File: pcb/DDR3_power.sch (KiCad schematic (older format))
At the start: 14 parts

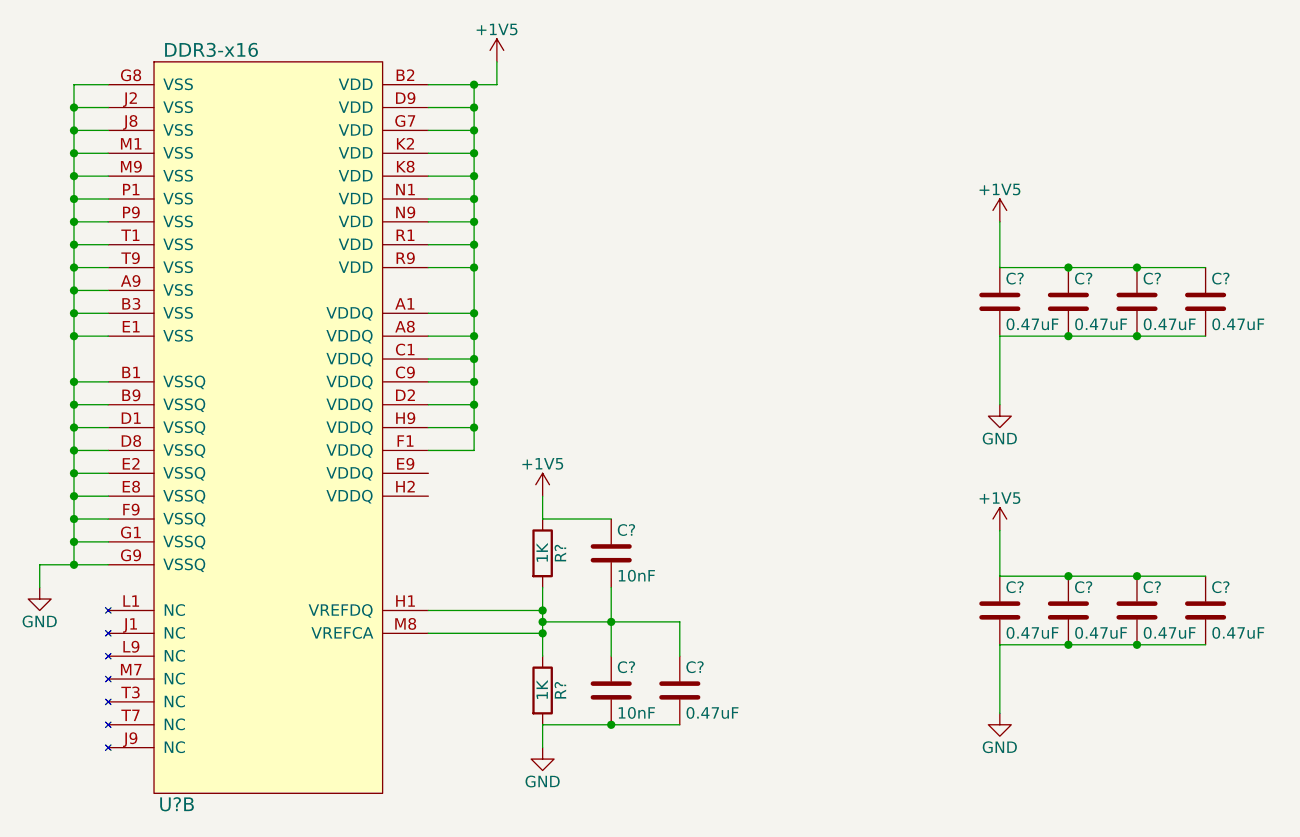
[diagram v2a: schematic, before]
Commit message: Added part numbers and updated schematic
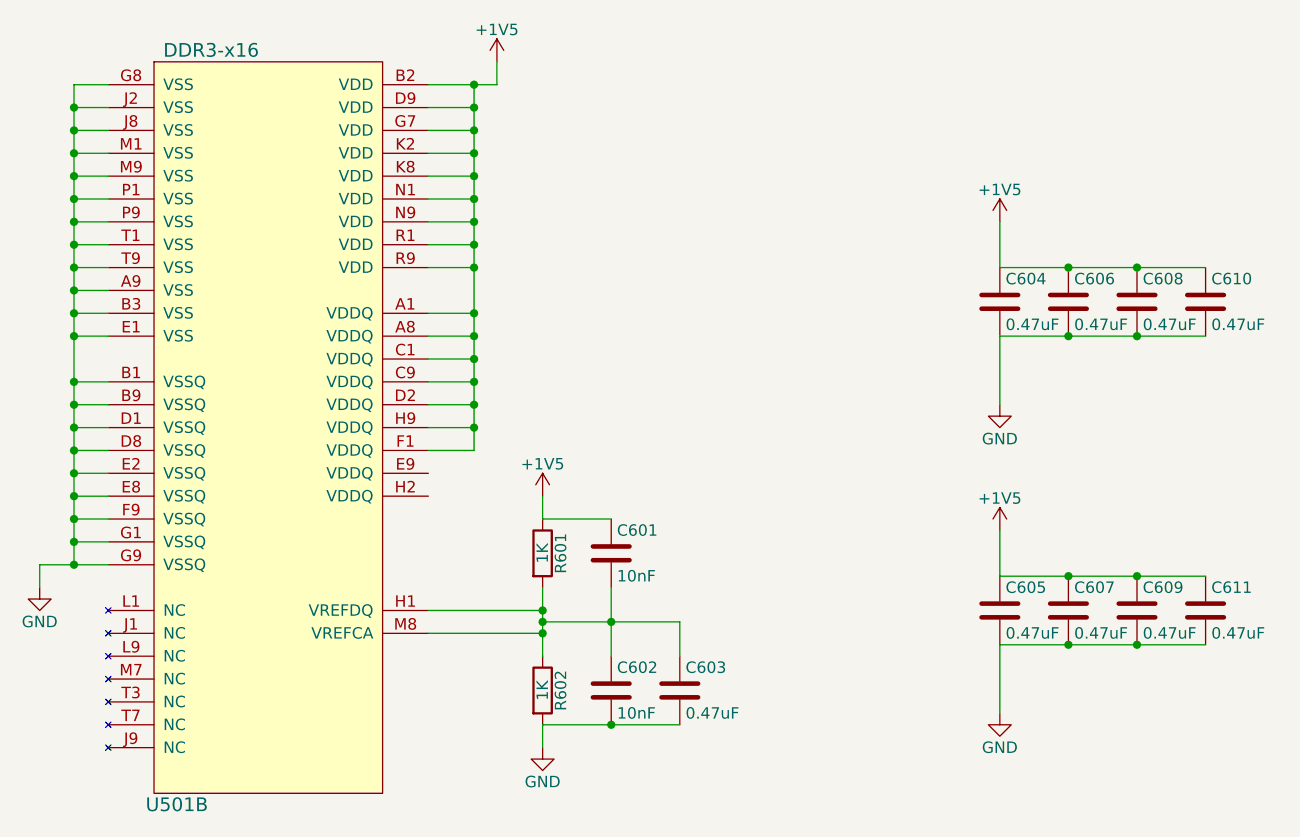
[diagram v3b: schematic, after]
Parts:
- gave numbers to parts that had none: 14
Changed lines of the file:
@@
 $EndDescr
 $Comp
-L DDR3-x16 U?
+L DDR3-x16 U501
 U 2 1 561B3BA2
 P 4900 3500
-F 0 "U?" H 4500 1850 60  0000 C CNN
+F 0 "U501" H 4500 1850 60  0000 C CNN
 F 1 "DDR3-x16" H 4650 5150 60  0000 C CNN
 F 2 "" H 4900 3100 60  0000 C CNN
@@
 Connection ~ 5800 2100
 $Comp
-L R R?
+L R R601
 U 1 1 561BF16C
 P 6100 4050
-F 0 "R?" V 6180 4050 50  0000 C CNN
+F 0 "R601" V 6180 4050 50  0000 C CNN
 F 1 "1K" V 6100 4050 50  0000 C CNN
 F 2 "" V 6030 4050 30  0000 C CNN
@@
 $EndComp
 $Comp
-L R R?
+L R R602
 U 1 1 561BF1C9
 P 6100 4650
-F 0 "R?" V 6180 4650 50  0000 C CNN
+F 0 "R602" V 6180 4650 50  0000 C CNN
 F 1 "1K" V 6100 4650 50  0000 C CNN
 F 2 "" V 6030 4650 30  0000 C CNN
@@
 $EndComp
 $Comp
-L C C?
+L C C601
 U 1 1 561BF214
 P 6400 4050
-F 0 "C?" H 6425 4150 50  0000 L CNN
+F 0 "C601" H 6425 4150 50  0000 L CNN
 F 1 "10nF" H 6425 3950 50  0000 L CNN
 F 2 "" H 6438 3900 30  0000 C CNN
@@
 $EndComp
 $Comp
-L C C?
+L C C602
 U 1 1 561BF25B
 P 6400 4650
-F 0 "C?" H 6425 4750 50  0000 L CNN
+F 0 "C602" H 6425 4750 50  0000 L CNN
 F 1 "10nF" H 6425 4550 50  0000 L CNN
 F 2 "" H 6438 4500 30  0000 C CNN
@@
 $EndComp
 $Comp
-L C C?
+L C C603
 U 1 1 561BF2A8
 P 6700 4650
-F 0 "C?" H 6725 4750 50  0000 L CNN
+F 0 "C603" H 6725 4750 50  0000 L CNN
 F 1 "0.47uF" H 6725 4550 50  0000 L CNN
 F 2 "" H 6738 4500 30  0000 C CNN
@@
 $EndComp
 $Comp
-L GND #PWR?
+L GND #PWR601
 U 1 1 561BF2F5
 P 3900 4200
-F 0 "#PWR?" H 3900 3950 50  0001 C CNN
+F 0 "#PWR601" H 3900 3950 50  0001 C CNN
 F 1 "GND" H 3900 4050 50  0000 C CNN
 F 2 "" H 3900 4200 60  0000 C CNN
@@
 $EndComp
 $Comp
-L GND #PWR?
+L GND #PWR604
 U 1 1 561BF315
 P 6100 4900
-F 0 "#PWR?" H 6100 4650 50  0001 C CNN
+F 0 "#PWR604" H 6100 4650 50  0001 C CNN
 F 1 "GND" H 6100 4750 50  0000 C CNN
 F 2 "" H 6100 4900 60  0000 C CNN
@@
 $EndComp
 $Comp
-L +1V5 #PWR?
+L +1V5 #PWR602
 U 1 1 561BF335
 P 5900 1900
-F 0 "#PWR?" H 5900 1750 50  0001 C CNN
+F 0 "#PWR602" H 5900 1750 50  0001 C CNN
 F 1 "+1V5" H 5900 2040 50  0000 C CNN
 F 2 "" H 5900 1900 60  0000 C CNN
@@
 $EndComp
 $Comp
-L +1V5 #PWR?
+L +1V5 #PWR603
 U 1 1 561BF355
 P 6100 3800
-F 0 "#PWR?" H 6100 3650 50  0001 C CNN
+F 0 "#PWR603" H 6100 3650 50  0001 C CNN
 F 1 "+1V5" H 6100 3940 50  0000 C CNN
 F 2 "" H 6100 3800 60  0000 C CNN
@@
 $EndComp
 $Comp
-L +1V5 #PWR?
+L +1V5 #PWR605
 U 1 1 561BF375
 P 8100 2600
-F 0 "#PWR?" H 8100 2450 50  0001 C CNN
+F 0 "#PWR605" H 8100 2450 50  0001 C CNN
 F 1 "+1V5" H 8100 2740 50  0000 C CNN
 F 2 "" H 8100 2600 60  0000 C CNN
@@
 $EndComp
 $Comp
-L GND #PWR?
+L GND #PWR606
 U 1 1 561BF395
 P 8100 3400
-F 0 "#PWR?" H 8100 3150 50  0001 C CNN
+F 0 "#PWR606" H 8100 3150 50  0001 C CNN
 F 1 "GND" H 8100 3250 50  0000 C CNN
 F 2 "" H 8100 3400 60  0000 C CNN
@@
 $EndComp
 $Comp
-L C C?
+L C C604
 U 1 1 561BF3B5
 P 8100 2950
-F 0 "C?" H 8125 3050 50  0000 L CNN
+F 0 "C604" H 8125 3050 50  0000 L CNN
 F 1 "0.47uF" H 8125 2850 50  0000 L CNN
 F 2 "" H 8138 2800 30  0000 C CNN
@@
 $EndComp
 $Comp
-L C C?
+L C C606
 U 1 1 561BF426
 P 8400 2950
-F 0 "C?" H 8425 3050 50  0000 L CNN
+F 0 "C606" H 8425 3050 50  0000 L CNN
 F 1 "0.47uF" H 8425 2850 50  0000 L CNN
 F 2 "" H 8438 2800 30  0000 C CNN
@@
 $EndComp
 $Comp
-L C C?
+L C C608
 U 1 1 561BF471
 P 8700 2950
-F 0 "C?" H 8725 3050 50  0000 L CNN
+F 0 "C608" H 8725 3050 50  0000 L CNN
 F 1 "0.47uF" H 8725 2850 50  0000 L CNN
 F 2 "" H 8738 2800 30  0000 C CNN
@@
 $EndComp
 $Comp
-L C C?
+L C C610
 U 1 1 561BF4DA
 P 9000 2950
-F 0 "C?" H 9025 3050 50  0000 L CNN
+F 0 "C610" H 9025 3050 50  0000 L CNN
 F 1 "0.47uF" H 9025 2850 50  0000 L CNN
 F 2 "" H 9038 2800 30  0000 C CNN
@@
 Connection ~ 4050 4100
 $Comp
-L +1V5 #PWR?
+L +1V5 #PWR607
 U 1 1 561C70D7
 P 8100 3950
-F 0 "#PWR?" H 8100 3800 50  0001 C CNN
+F 0 "#PWR607" H 8100 3800 50  0001 C CNN
 F 1 "+1V5" H 8100 4090 50  0000 C CNN
 F 2 "" H 8100 3950 60  0000 C CNN
@@
 $EndComp
 $Comp
-L GND #PWR?
+L GND #PWR608
 U 1 1 561C70DD
 P 8100 4750
-F 0 "#PWR?" H 8100 4500 50  0001 C CNN
+F 0 "#PWR608" H 8100 4500 50  0001 C CNN
 F 1 "GND" H 8100 4600 50  0000 C CNN
 F 2 "" H 8100 4750 60  0000 C CNN
@@
 $EndComp
 $Comp
-L C C?
+L C C605
 U 1 1 561C70E3
 P 8100 4300
-F 0 "C?" H 8125 4400 50  0000 L CNN
+F 0 "C605" H 8125 4400 50  0000 L CNN
 F 1 "0.47uF" H 8125 4200 50  0000 L CNN
 F 2 "" H 8138 4150 30  0000 C CNN
@@
 $EndComp
 $Comp
-L C C?
+L C C607
 U 1 1 561C70E9
 P 8400 4300
-F 0 "C?" H 8425 4400 50  0000 L CNN
+F 0 "C607" H 8425 4400 50  0000 L CNN
 F 1 "0.47uF" H 8425 4200 50  0000 L CNN
 F 2 "" H 8438 4150 30  0000 C CNN
@@
 $EndComp
 $Comp
-L C C?
+L C C609
 U 1 1 561C70EF
 P 8700 4300
-F 0 "C?" H 8725 4400 50  0000 L CNN
+F 0 "C609" H 8725 4400 50  0000 L CNN
 F 1 "0.47uF" H 8725 4200 50  0000 L CNN
 F 2 "" H 8738 4150 30  0000 C CNN
@@
 $EndComp
 $Comp
-L C C?
+L C C611
 U 1 1 561C70F5
 P 9000 4300
-F 0 "C?" H 9025 4400 50  0000 L CNN
+F 0 "C611" H 9025 4400 50  0000 L CNN
 F 1 "0.47uF" H 9025 4200 50  0000 L CNN
 F 2 "" H 9038 4150 30  0000 C CNN

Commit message: mostly done with component placement
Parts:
- C601, C602, C603, C604, C605, C606, C607, C608, C609, C610, C611: footprint (none) -> wbraun_smd:C_0402
- R601, R602: footprint (none) -> wbraun_smd:R_0402
- U501: footprint (none) -> wbraun_smd:FBGA-96-DDR3-SDRAM
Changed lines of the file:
@@
 F 0 "U501" H 4500 1850 60  0000 C CNN
 F 1 "DDR3-x16" H 4650 5150 60  0000 C CNN
-F 2 "" H 4900 3100 60  0000 C CNN
+F 2 "wbraun_smd:FBGA-96-DDR3-SDRAM" H 4900 3100 60  0001 C CNN
 F 3 "" H 4900 3100 60  0000 C CNN
 	2    4900 3500
@@
 F 0 "R601" V 6180 4050 50  0000 C CNN
 F 1 "1K" V 6100 4050 50  0000 C CNN
-F 2 "" V 6030 4050 30  0000 C CNN
+F 2 "wbraun_smd:R_0402" V 6030 4050 30  0001 C CNN
 F 3 "" H 6100 4050 30  0000 C CNN
 	1    6100 4050
@@
 F 0 "R602" V 6180 4650 50  0000 C CNN
 F 1 "1K" V 6100 4650 50  0000 C CNN
-F 2 "" V 6030 4650 30  0000 C CNN
+F 2 "wbraun_smd:R_0402" V 6030 4650 30  0001 C CNN
 F 3 "" H 6100 4650 30  0000 C CNN
 	1    6100 4650
@@
 F 0 "C601" H 6425 4150 50  0000 L CNN
 F 1 "10nF" H 6425 3950 50  0000 L CNN
-F 2 "" H 6438 3900 30  0000 C CNN
+F 2 "wbraun_smd:C_0402" H 6438 3900 30  0001 C CNN
 F 3 "" H 6400 4050 60  0000 C CNN
 	1    6400 4050
@@
 F 0 "C602" H 6425 4750 50  0000 L CNN
 F 1 "10nF" H 6425 4550 50  0000 L CNN
-F 2 "" H 6438 4500 30  0000 C CNN
+F 2 "wbraun_smd:C_0402" H 6438 4500 30  0001 C CNN
 F 3 "" H 6400 4650 60  0000 C CNN
 	1    6400 4650
@@
 F 0 "C603" H 6725 4750 50  0000 L CNN
 F 1 "0.47uF" H 6725 4550 50  0000 L CNN
-F 2 "" H 6738 4500 30  0000 C CNN
+F 2 "wbraun_smd:C_0402" H 6738 4500 30  0001 C CNN
 F 3 "" H 6700 4650 60  0000 C CNN
 	1    6700 4650
@@
 $EndComp
 $Comp
-L GND #PWR601
+L GND #PWR081
 U 1 1 561BF2F5
 P 3900 4200
-F 0 "#PWR601" H 3900 3950 50  0001 C CNN
+F 0 "#PWR081" H 3900 3950 50  0001 C CNN
 F 1 "GND" H 3900 4050 50  0000 C CNN
 F 2 "" H 3900 4200 60  0000 C CNN
@@
 $EndComp
 $Comp
-L GND #PWR604
+L GND #PWR082
 U 1 1 561BF315
 P 6100 4900
-F 0 "#PWR604" H 6100 4650 50  0001 C CNN
+F 0 "#PWR082" H 6100 4650 50  0001 C CNN
 F 1 "GND" H 6100 4750 50  0000 C CNN
 F 2 "" H 6100 4900 60  0000 C CNN
@@
 $EndComp
 $Comp
-L +1V5 #PWR602
+L +1V5 #PWR083
 U 1 1 561BF335
 P 5900 1900
-F 0 "#PWR602" H 5900 1750 50  0001 C CNN
+F 0 "#PWR083" H 5900 1750 50  0001 C CNN
 F 1 "+1V5" H 5900 2040 50  0000 C CNN
 F 2 "" H 5900 1900 60  0000 C CNN
@@
 $EndComp
 $Comp
-L +1V5 #PWR603
+L +1V5 #PWR084
 U 1 1 561BF355
 P 6100 3800
-F 0 "#PWR603" H 6100 3650 50  0001 C CNN
+F 0 "#PWR084" H 6100 3650 50  0001 C CNN
 F 1 "+1V5" H 6100 3940 50  0000 C CNN
 F 2 "" H 6100 3800 60  0000 C CNN
@@
 $EndComp
 $Comp
-L +1V5 #PWR605
+L +1V5 #PWR085
 U 1 1 561BF375
 P 8100 2600
-F 0 "#PWR605" H 8100 2450 50  0001 C CNN
+F 0 "#PWR085" H 8100 2450 50  0001 C CNN
 F 1 "+1V5" H 8100 2740 50  0000 C CNN
 F 2 "" H 8100 2600 60  0000 C CNN
@@
 $EndComp
 $Comp
-L GND #PWR606
+L GND #PWR086
 U 1 1 561BF395
 P 8100 3400
-F 0 "#PWR606" H 8100 3150 50  0001 C CNN
+F 0 "#PWR086" H 8100 3150 50  0001 C CNN
 F 1 "GND" H 8100 3250 50  0000 C CNN
 F 2 "" H 8100 3400 60  0000 C CNN
@@
 F 0 "C604" H 8125 3050 50  0000 L CNN
 F 1 "0.47uF" H 8125 2850 50  0000 L CNN
-F 2 "" H 8138 2800 30  0000 C CNN
+F 2 "wbraun_smd:C_0402" H 8138 2800 30  0001 C CNN
 F 3 "" H 8100 2950 60  0000 C CNN
 	1    8100 2950
@@
 F 0 "C606" H 8425 3050 50  0000 L CNN
 F 1 "0.47uF" H 8425 2850 50  0000 L CNN
-F 2 "" H 8438 2800 30  0000 C CNN
+F 2 "wbraun_smd:C_0402" H 8438 2800 30  0001 C CNN
 F 3 "" H 8400 2950 60  0000 C CNN
 	1    8400 2950
@@
 F 0 "C608" H 8725 3050 50  0000 L CNN
 F 1 "0.47uF" H 8725 2850 50  0000 L CNN
-F 2 "" H 8738 2800 30  0000 C CNN
+F 2 "wbraun_smd:C_0402" H 8738 2800 30  0001 C CNN
 F 3 "" H 8700 2950 60  0000 C CNN
 	1    8700 2950
@@
 F 0 "C610" H 9025 3050 50  0000 L CNN
 F 1 "0.47uF" H 9025 2850 50  0000 L CNN
-F 2 "" H 9038 2800 30  0000 C CNN
+F 2 "wbraun_smd:C_0402" H 9038 2800 30  0001 C CNN
 F 3 "" H 9000 2950 60  0000 C CNN
 	1    9000 2950
@@
 Connection ~ 4050 4100
 $Comp
-L +1V5 #PWR607
+L +1V5 #PWR087
 U 1 1 561C70D7
 P 8100 3950
-F 0 "#PWR607" H 8100 3800 50  0001 C CNN
+F 0 "#PWR087" H 8100 3800 50  0001 C CNN
 F 1 "+1V5" H 8100 4090 50  0000 C CNN
 F 2 "" H 8100 3950 60  0000 C CNN
@@
 $EndComp
 $Comp
-L GND #PWR608
+L GND #PWR088
 U 1 1 561C70DD
 P 8100 4750
-F 0 "#PWR608" H 8100 4500 50  0001 C CNN
+F 0 "#PWR088" H 8100 4500 50  0001 C CNN
 F 1 "GND" H 8100 4600 50  0000 C CNN
 F 2 "" H 8100 4750 60  0000 C CNN
@@
 F 0 "C605" H 8125 4400 50  0000 L CNN
 F 1 "0.47uF" H 8125 4200 50  0000 L CNN
-F 2 "" H 8138 4150 30  0000 C CNN
+F 2 "wbraun_smd:C_0402" H 8138 4150 30  0001 C CNN
 F 3 "" H 8100 4300 60  0000 C CNN
 	1    8100 4300
@@
 F 0 "C607" H 8425 4400 50  0000 L CNN
 F 1 "0.47uF" H 8425 4200 50  0000 L CNN
-F 2 "" H 8438 4150 30  0000 C CNN
+F 2 "wbraun_smd:C_0402" H 8438 4150 30  0001 C CNN
 F 3 "" H 8400 4300 60  0000 C CNN
 	1    8400 4300
@@
 F 0 "C609" H 8725 4400 50  0000 L CNN
 F 1 "0.47uF" H 8725 4200 50  0000 L CNN
-F 2 "" H 8738 4150 30  0000 C CNN
+F 2 "wbraun_smd:C_0402" H 8738 4150 30  0001 C CNN
 F 3 "" H 8700 4300 60  0000 C CNN
 	1    8700 4300
@@
 F 0 "C611" H 9025 4400 50  0000 L CNN
 F 1 "0.47uF" H 9025 4200 50  0000 L CNN
-F 2 "" H 9038 4150 30  0000 C CNN
+F 2 "wbraun_smd:C_0402" H 9038 4150 30  0001 C CNN
 F 3 "" H 9000 4300 60  0000 C CNN
 	1    9000 4300

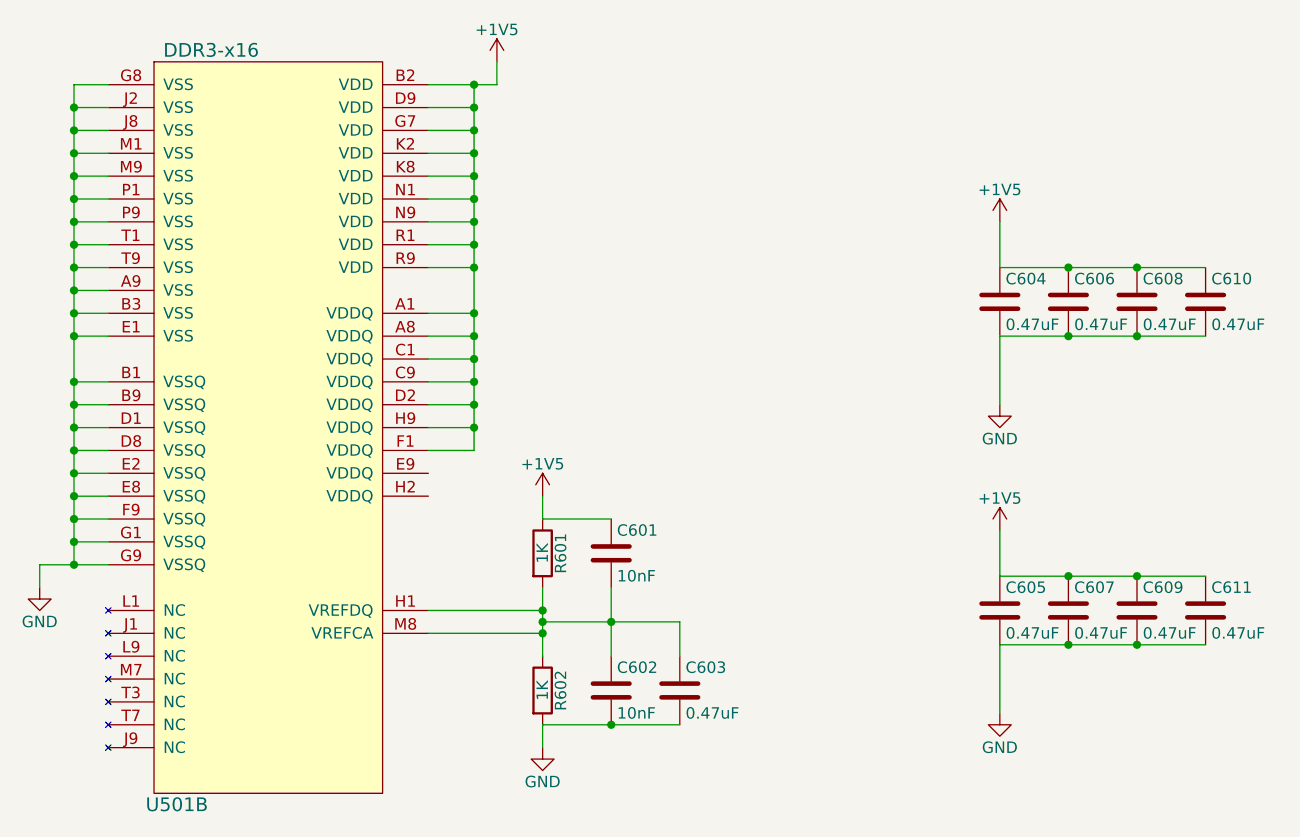
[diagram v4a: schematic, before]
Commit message: DDR routing test 1
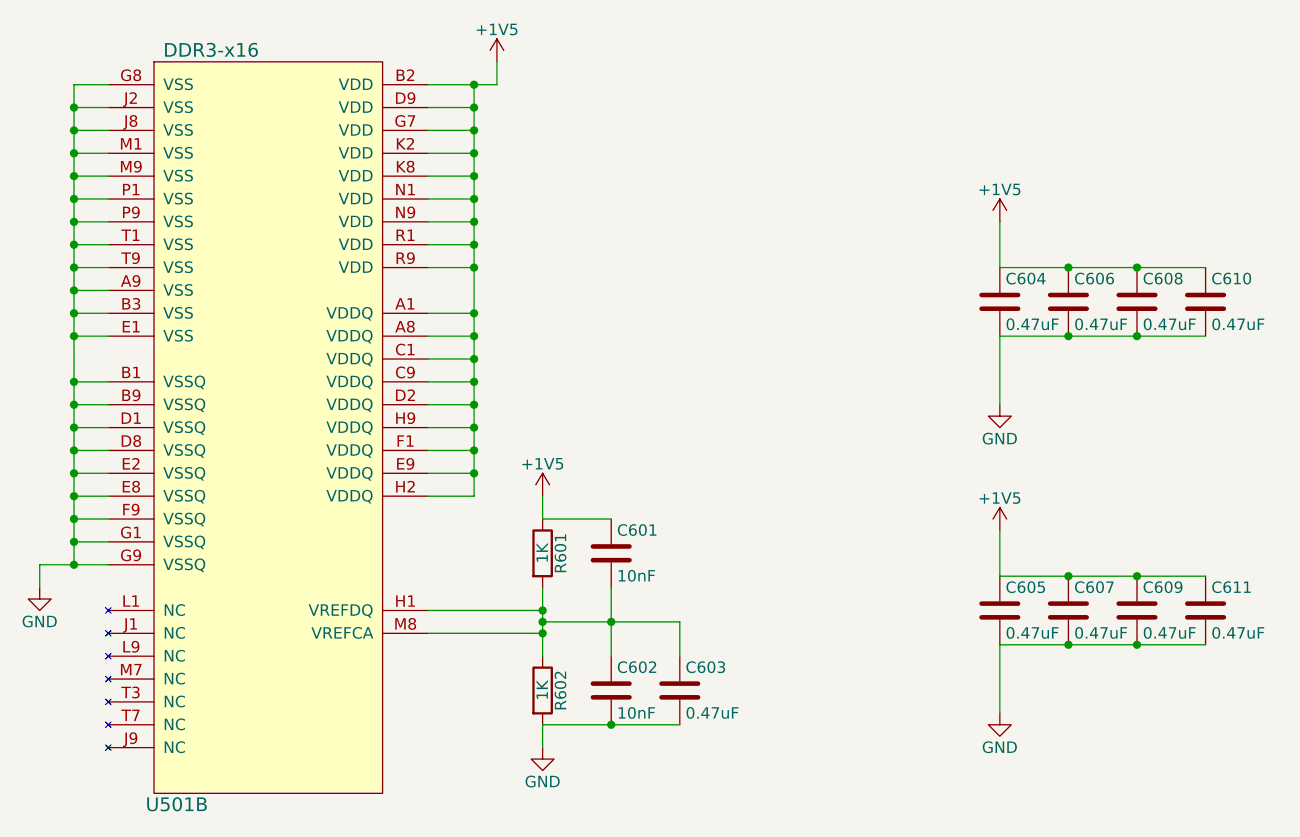
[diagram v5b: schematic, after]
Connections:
- net +1V5: now also U501.E9 (VDDQ), U501.H2 (VDDQ)
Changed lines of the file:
@@
 $Descr A4 11693 8268
 encoding utf-8
-Sheet 6 12
+Sheet 6 13
 Title ""
 Date ""
@@
 	5600 2000 5900 2000
 Wire Wire Line
-	5800 2000 5800 3600
+	5800 2000 5800 3800
 Wire Wire Line
 	5800 2800 5600 2800
@@
 Wire Wire Line
 	8100 4450 8100 4750
+Wire Wire Line
+	5800 3700 5600 3700
+Connection ~ 5800 3600
+Wire Wire Line
+	5800 3800 5600 3800
+Connection ~ 5800 3700
 $EndSCHEMATC
